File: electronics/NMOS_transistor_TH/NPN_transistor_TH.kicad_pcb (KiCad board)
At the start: 2 copper layers, 19 x 19 mm, 7 parts, among them J1 B, J2 E, J3 C, J4 E, Q1 BC547

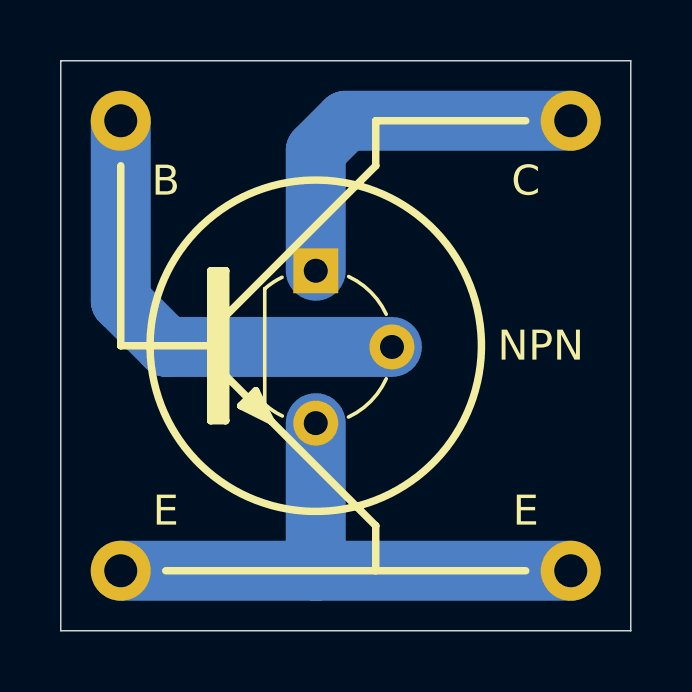
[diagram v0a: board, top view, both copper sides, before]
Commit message: changed to bit wider footprint
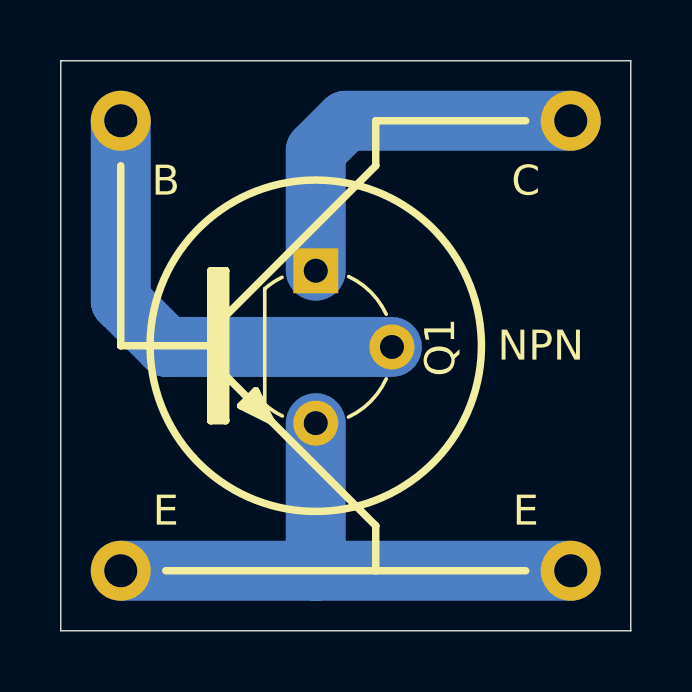
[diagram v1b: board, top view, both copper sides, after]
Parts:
- N1: value 20201118 -> 20201122
- Q1: value BC547 -> Q_NMOS_DGS
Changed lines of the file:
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@@
   )
   (setup
-    (last_trace_width 2)
+    (last_trace_width 0.25)
     (user_trace_width 0.2)
     (user_trace_width 0.3)
@@
     (descr "TO-92L leads in-line (large body variant of TO-92), also known as TO-226, wide, drill 0.75mm (see https://www.diodes.com/assets/Package-Files/TO92L.pdf and http://www.ti.com/lit/an/snoa059/snoa059.pdf)")
     (tags "TO-92L Molded Wide transistor")
-    (fp_text reference Q1 (at 2.55 -4.15 90) (layer F.Fab)
-      (effects (font (size 1 1) (thickness 0.15)))
-    )
-    (fp_text value BC547 (at 2.54 2.79 90) (layer F.Fab)
+    (fp_text reference Q1 (at 2.55 -4.15 90) (layer F.SilkS)
+      (effects (font (size 1 1) (thickness 0.15)))
+    )
+    (fp_text value Q_NMOS_DGS (at 2.54 2.79 90) (layer F.Fab)
       (effects (font (size 1 1) (thickness 0.15)))
     )
@@
       (effects (font (size 1 1) (thickness 0.15)))
     )
-    (fp_circle (center 0 0) (end 1.3 0) (layer B.CrtYd) (width 0.025))
-    (fp_circle (center 0 0) (end 1.3 0) (layer F.CrtYd) (width 0.025))
+    (fp_circle (center 0 0) (end 1.3 0) (layer F.CrtYd) (width 0.025))
+    (fp_circle (center 0 0) (end 1.3 0) (layer B.CrtYd) (width 0.025))
     (pad 1 thru_hole circle (at 0 0) (size 2 2) (drill 1.1) (layers *.Cu *.Mask)
       (net 2 "Net-(J2-Pad1)"))
@@
       (effects (font (size 1 1) (thickness 0.15)))
     )
-    (fp_circle (center 0 0) (end 1.3 0) (layer B.CrtYd) (width 0.025))
-    (fp_circle (center 0 0) (end 1.3 0) (layer F.CrtYd) (width 0.025))
+    (fp_circle (center 0 0) (end 1.3 0) (layer F.CrtYd) (width 0.025))
+    (fp_circle (center 0 0) (end 1.3 0) (layer B.CrtYd) (width 0.025))
     (pad 1 thru_hole circle (at 0 0) (size 2 2) (drill 1.1) (layers *.Cu *.Mask)
       (net 3 "Net-(J3-Pad1)"))
@@
       (effects (font (size 1 1) (thickness 0.15)))
     )
-    (fp_circle (center 0 0) (end 1.3 0) (layer B.CrtYd) (width 0.025))
-    (fp_circle (center 0 0) (end 1.3 0) (layer F.CrtYd) (width 0.025))
+    (fp_circle (center 0 0) (end 1.3 0) (layer F.CrtYd) (width 0.025))
+    (fp_circle (center 0 0) (end 1.3 0) (layer B.CrtYd) (width 0.025))
     (pad 1 thru_hole circle (at 0 0) (size 2 2) (drill 1.1) (layers *.Cu *.Mask)
       (net 2 "Net-(J2-Pad1)"))
@@
       (effects (font (size 1 1) (thickness 0.15)))
     )
-    (fp_circle (center 0 0) (end 1.3 0) (layer B.CrtYd) (width 0.025))
-    (fp_circle (center 0 0) (end 1.3 0) (layer F.CrtYd) (width 0.025))
+    (fp_circle (center 0 0) (end 1.3 0) (layer F.CrtYd) (width 0.025))
+    (fp_circle (center 0 0) (end 1.3 0) (layer B.CrtYd) (width 0.025))
     (pad 1 thru_hole circle (at 0 0) (size 2 2) (drill 1.1) (layers *.Cu *.Mask)
       (net 1 "Net-(J1-Pad1)"))
@@
       (effects (font (size 1 1) (thickness 0.15)) (justify mirror))
     )
-    (fp_text value 20201118 (at 0.8 0.1 90) (layer B.SilkS)
+    (fp_text value 20201122 (at 0.8 0.1 90) (layer B.SilkS)
       (effects (font (size 0.8 0.8) (thickness 0.15)) (justify mirror))
     )

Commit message: routed and completed NMOS silk artwork
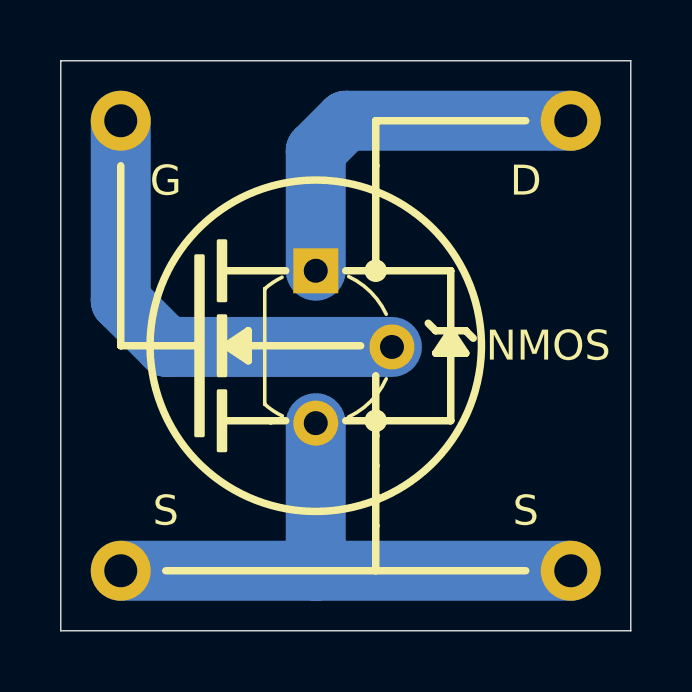
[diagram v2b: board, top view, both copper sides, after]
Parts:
- J1: value B -> G
- J2, J4: value E -> S
- J3: value C -> D
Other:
- board text added: "NMOS"
- board text removed: "NPN"
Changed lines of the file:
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@@
   (general
     (thickness 1.6)
-    (drawings 24)
+    (drawings 43)
     (tracks 9)
     (zones 0)
@@
     (descr "TO-92L leads in-line (large body variant of TO-92), also known as TO-226, wide, drill 0.75mm (see https://www.diodes.com/assets/Package-Files/TO92L.pdf and http://www.ti.com/lit/an/snoa059/snoa059.pdf)")
     (tags "TO-92L Molded Wide transistor")
-    (fp_text reference Q1 (at 2.55 -4.15 90) (layer F.SilkS)
+    (fp_text reference Q1 (at 2.54 0 270) (layer F.Fab)
       (effects (font (size 1 1) (thickness 0.15)))
     )
@@
       (effects (font (size 1 1) (thickness 0.15)))
     )
-    (fp_text value E (at -1.5 -2) (layer F.SilkS)
+    (fp_text value S (at -1.5 -2) (layer F.SilkS)
       (effects (font (size 1 1) (thickness 0.15)))
     )
@@
       (effects (font (size 1 1) (thickness 0.15)))
     )
-    (fp_text value C (at -1.5 2) (layer F.SilkS)
+    (fp_text value D (at -1.5 2) (layer F.SilkS)
       (effects (font (size 1 1) (thickness 0.15)))
     )
@@
       (effects (font (size 1 1) (thickness 0.15)))
     )
-    (fp_text value E (at 1.5 -2) (layer F.SilkS)
+    (fp_text value S (at 1.5 -2) (layer F.SilkS)
       (effects (font (size 1 1) (thickness 0.15)))
     )
@@
       (effects (font (size 1 1) (thickness 0.15)))
     )
-    (fp_text value B (at 1.5 2) (layer F.SilkS)
+    (fp_text value G (at 1.5 2) (layer F.SilkS)
       (effects (font (size 1 1) (thickness 0.15)))
     )
@@
     (fp_line (start -0.5 -0.6) (end 0.5 -0.6) (layer B.SilkS) (width 0.15))
   )
-  (gr_poly (pts (xy 147 73) (xy 146 72.5) (xy 146.5 72)) (layer F.SilkS) (width 0.1))
-  (gr_poly (pts (xy 145.5 73) (xy 145 73) (xy 145 68) (xy 145.5 68)) (layer F.SilkS) (width 0.1))
-  (gr_line (start 146 72.5) (end 147 73) (layer F.SilkS) (width 0.25))
-  (gr_line (start 146.5 72) (end 146 72.5) (layer F.SilkS) (width 0.25))
-  (gr_line (start 147 73) (end 146.5 72) (layer F.SilkS) (width 0.25))
+  (gr_line (start 150.5 73) (end 149.5 73) (layer F.SilkS) (width 0.25))
+  (gr_line (start 147 73) (end 147.5 73) (layer F.SilkS) (width 0.25))
+  (gr_line (start 153 68) (end 149.5 68) (layer F.SilkS) (width 0.25))
+  (gr_poly (pts (xy 146.25 71) (xy 145.5 70.5) (xy 146.25 70)) (layer F.SilkS) (width 0.1))
+  (gr_line (start 142 70.5) (end 144.5 70.5) (layer F.SilkS) (width 0.25))
+  (gr_line (start 150.5 64.5) (end 150.5 68) (layer F.SilkS) (width 0.25))
+  (gr_circle (center 150.5 68) (end 150.75 68) (layer F.SilkS) (width 0.25))
+  (gr_poly (pts (xy 153.5 70.75) (xy 152.5 70.75) (xy 153 70)) (layer F.SilkS) (width 0.1))
+  (gr_line (start 153.5 70) (end 153.75 70.25) (layer F.SilkS) (width 0.25))
+  (gr_line (start 152.5 70) (end 152.25 69.75) (layer F.SilkS) (width 0.25))
+  (gr_line (start 152.5 70) (end 153.5 70) (layer F.SilkS) (width 0.25))
+  (gr_line (start 152.5 70.75) (end 153 70) (layer F.SilkS) (width 0.25))
+  (gr_line (start 153.5 70.75) (end 152.5 70.75) (layer F.SilkS) (width 0.25))
+  (gr_line (start 153 70) (end 153.5 70.75) (layer F.SilkS) (width 0.25))
+  (gr_circle (center 150.5 73) (end 150.75 73) (layer F.SilkS) (width 0.25))
+  (gr_line (start 150.5 73.25) (end 150.5 73) (layer F.SilkS) (width 0.25))
+  (gr_line (start 150.5 71.5) (end 150.5 73.25) (layer F.SilkS) (width 0.25))
+  (gr_line (start 145.5 70.5) (end 150 70.5) (layer F.SilkS) (width 0.25))
+  (gr_line (start 146.25 71) (end 145.5 70.5) (layer F.SilkS) (width 0.25))
+  (gr_line (start 146.25 70) (end 146.25 71) (layer F.SilkS) (width 0.25))
+  (gr_line (start 145.5 70.5) (end 146.25 70) (layer F.SilkS) (width 0.25))
+  (gr_line (start 147.5 68) (end 145.5 68) (layer F.SilkS) (width 0.25))
+  (gr_line (start 153 73) (end 153 68) (layer F.SilkS) (width 0.25))
+  (gr_line (start 150.5 73) (end 153 73) (layer F.SilkS) (width 0.25))
+  (gr_poly (pts (xy 145.5 74) (xy 145.25 74) (xy 145.25 72) (xy 145.5 72)) (layer F.SilkS) (width 0.1))
+  (gr_poly (pts (xy 145.5 71.5) (xy 145.25 71.5) (xy 145.25 69.5) (xy 145.5 69.5)) (layer F.SilkS) (width 0.1))
+  (gr_poly (pts (xy 145.5 69) (xy 145.25 69) (xy 145.25 67) (xy 145.5 67)) (layer F.SilkS) (width 0.1))
+  (gr_poly (pts (xy 144.75 73.5) (xy 144.5 73.5) (xy 144.5 67.5) (xy 144.75 67.5)) (layer F.SilkS) (width 0.1))
+  (gr_line (start 147 73) (end 145.5 73) (layer F.SilkS) (width 0.25))
+  (gr_line (start 150.5 73.5) (end 150.5 73) (layer F.SilkS) (width 0.25))
+  (gr_line (start 150.5 74.5) (end 150.5 73.5) (layer F.SilkS) (width 0.25))
+  (gr_line (start 150.5 76.5) (end 150.5 74.5) (layer F.SilkS) (width 0.25))
   (gr_line (start 150.5 63) (end 155.5 63) (layer F.SilkS) (width 0.25))
   (gr_line (start 150.5 64.5) (end 150.5 63) (layer F.SilkS) (width 0.25))
-  (gr_line (start 145 70) (end 150.5 64.5) (layer F.SilkS) (width 0.25))
-  (gr_line (start 150.5 76.5) (end 145 71) (layer F.SilkS) (width 0.25))
   (gr_line (start 150.5 78) (end 150.5 76.5) (layer F.SilkS) (width 0.25))
-  (gr_line (start 145 73) (end 145 70.5) (layer F.SilkS) (width 0.25))
-  (gr_line (start 145.5 73) (end 145 73) (layer F.SilkS) (width 0.25))
-  (gr_line (start 145.5 68) (end 145.5 73) (layer F.SilkS) (width 0.25))
-  (gr_line (start 145 68) (end 145.5 68) (layer F.SilkS) (width 0.25))
-  (gr_line (start 145 70.5) (end 145 68) (layer F.SilkS) (width 0.25))
-  (gr_line (start 142 70.5) (end 145 70.5) (layer F.SilkS) (width 0.25))
   (gr_line (start 142 64.5) (end 142 70.5) (layer F.SilkS) (width 0.25))
-  (gr_text NPN (at 156 70.5) (layer F.SilkS)
+  (gr_text NMOS (at 156.25 70.5) (layer F.SilkS)
     (effects (font (size 1 1) (thickness 0.15)))
   )
